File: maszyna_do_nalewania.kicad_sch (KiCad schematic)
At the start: 23 parts, among them J1 USB_C_Receptacle_USB2.0_16P, U1 ESP32-C3, Y1 40Mhz 10ppm

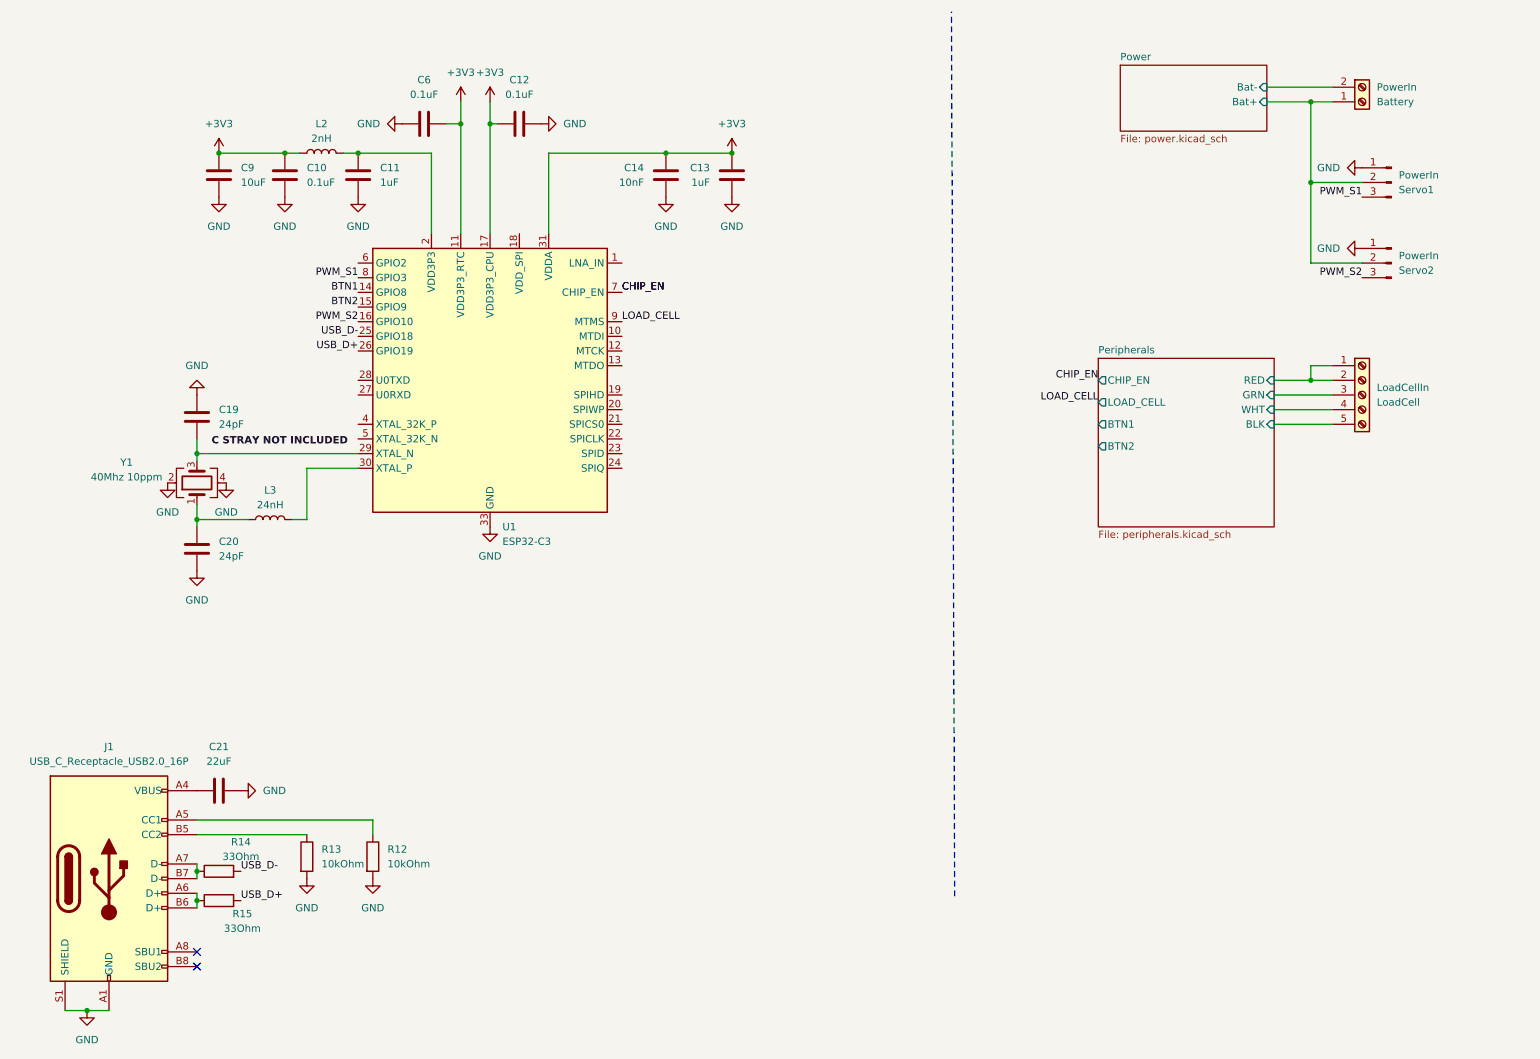
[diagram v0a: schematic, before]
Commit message: feat: led_inf connected, load cell overvoltage protection and antenna vals defined
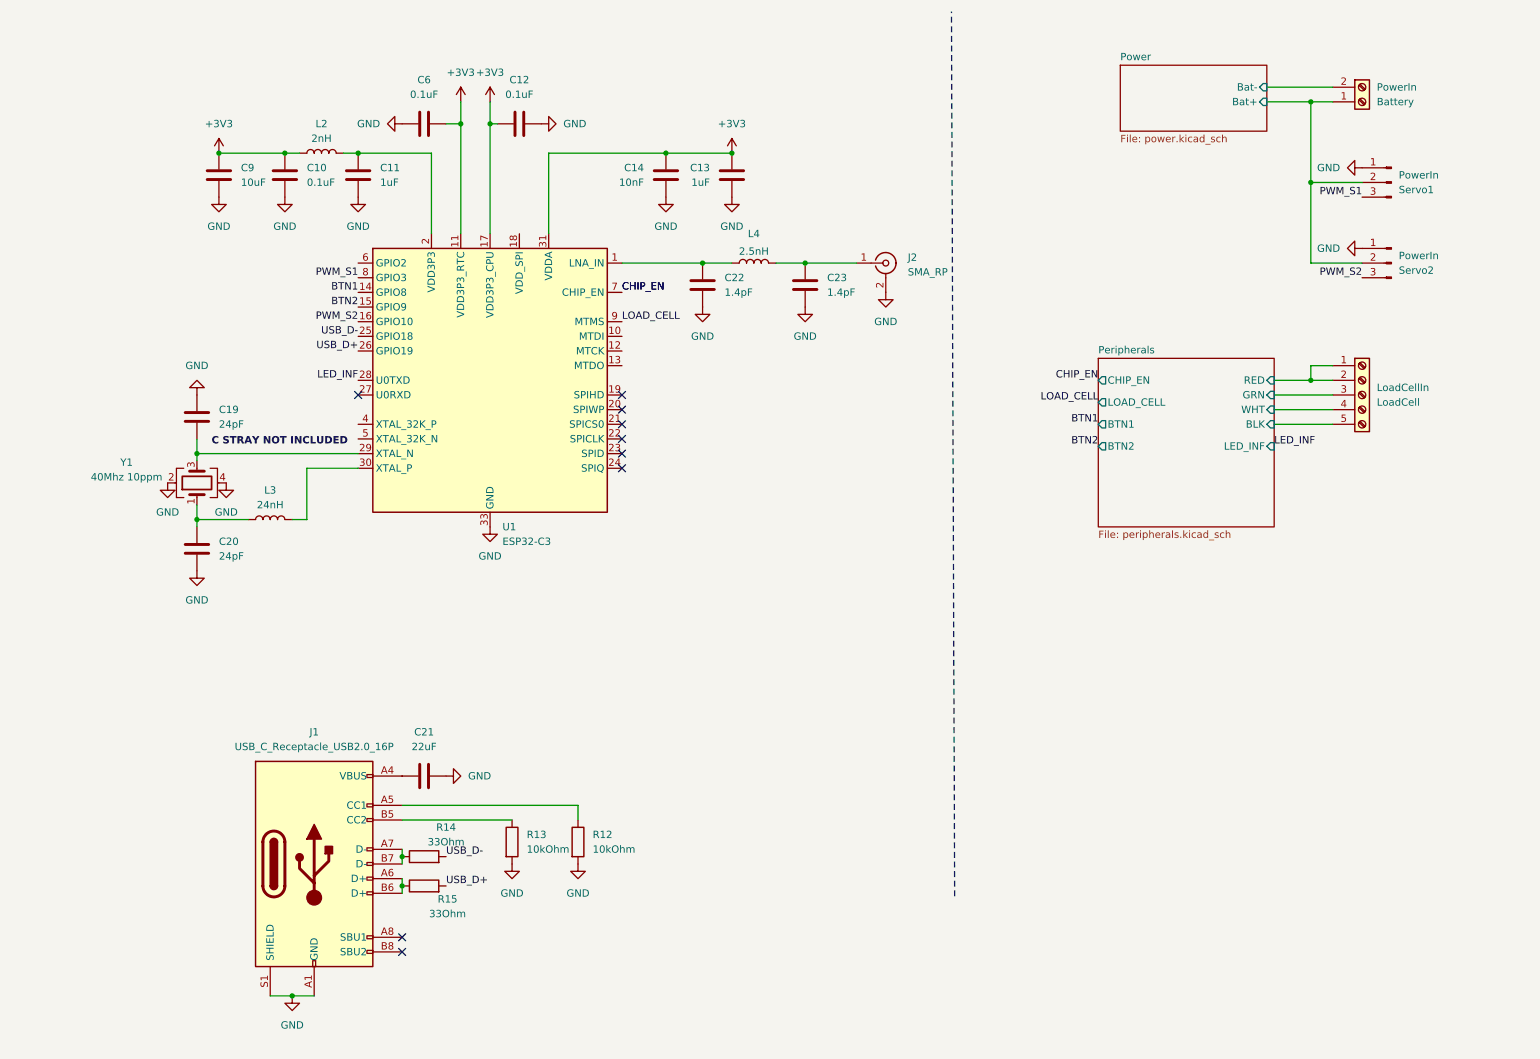
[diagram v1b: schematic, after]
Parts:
- added C22, C23: 1.4pF, Capacitor_SMD:C_0805_2012Metric_Pad1.18x1.45mm_HandSolder, symbol Device:C
- added J2: SMA_RP, Connector_Coaxial:SMA_Amphenol_132289_EdgeMount, symbol Connector:Conn_Coaxial
- added L4: 2.5nH, Inductor_SMD:L_0402_1005Metric_Pad0.77x0.64mm_HandSolder, symbol Device:L
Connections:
- net GND: now also C22.1, C23.1, J2.2 (Ext)
- net at U1.1 (LNA_IN): now also C22.2, L4.1
- net LED_INF: now reaches U1.28 (U0TXD)
- new net: C23.2, J2.1 (In), L4.2
- no-connect marks 2 -> 9
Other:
- sheet Peripherals ports: added LED_INF; removed none
- moved on the sheet: C21, J1, R12, R13, R14, R15

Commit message: feat: added power button, name changes
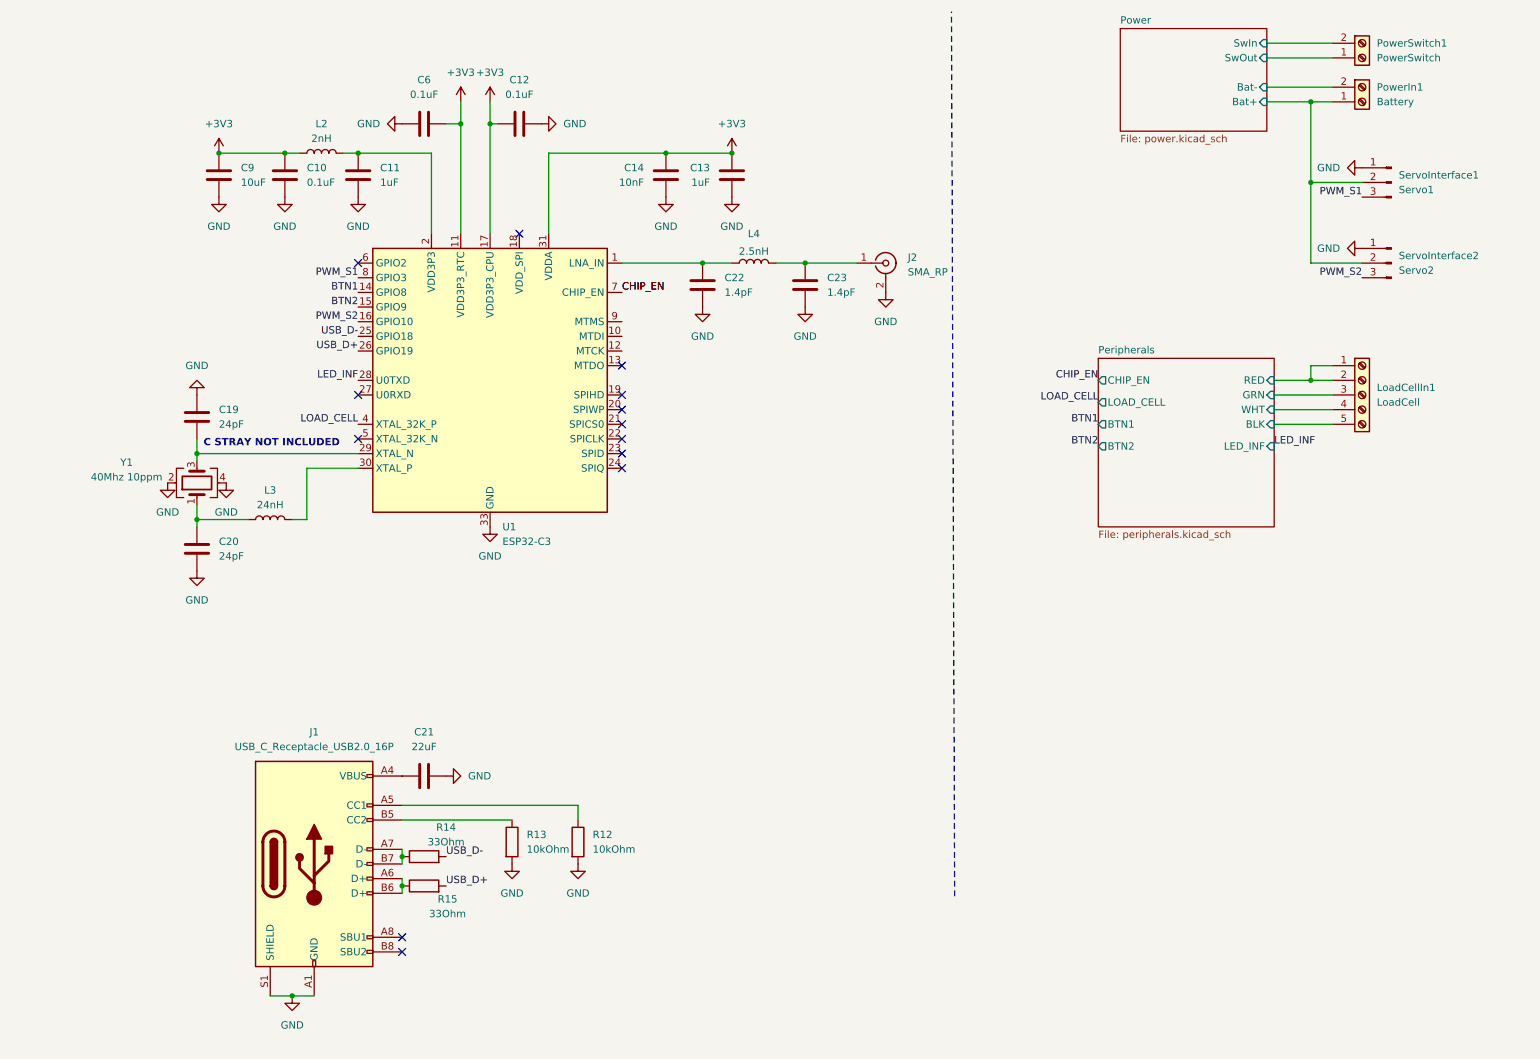
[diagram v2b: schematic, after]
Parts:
- removed LoadCellIn: LoadCell, symbol Connector:Screw_Terminal_01x05
- added LoadCellIn1: LoadCell, TerminalBlock:TerminalBlock_MaiXu_MX126-5.0-05P_1x05_P5.00mm, symbol Connector:Screw_Terminal_01x05
- added PowerSwitch1: PowerSwitch, TerminalBlock:TerminalBlock_MaiXu_MX126-5.0-02P_1x02_P5.00mm, symbol Connector:Screw_Terminal_01x02
- renumbered PowerIn to PowerIn1, PowerIn to ServoInterface1, PowerIn to ServoInterface2
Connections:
- net LOAD_CELL: now also U1.4 (XTAL_32K_P); no longer U1.9 (MTMS)
- net Peripherals/BLK: now also LoadCellIn1.5 (Pin_5)
- net Peripherals/GRN: now also LoadCellIn1.3 (Pin_3)
- net Peripherals/RED: now also LoadCellIn1.1 (Pin_1), LoadCellIn1.2 (Pin_2)
- net Peripherals/WHT: now also LoadCellIn1.4 (Pin_4)
- new net Power/SwIn: PowerSwitch1.2 (Pin_2)
- new net Power/SwOut: PowerSwitch1.1 (Pin_1)
- no-connect marks 9 -> 13
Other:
- sheet Power ports: added SwIn, SwOut; removed none
- note added: "C STRAY NOT INCLUDED"
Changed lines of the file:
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@@
 	(generator_version "9.0")
 	(paper "A4")
+	(text "C STRAY NOT INCLUDED"
+		(exclude_from_sim no)
+		(at 58.674 87.122 0)
+		(effects
+			(font
+				(size 1.27 1.27)
+				(thickness 0.254)
+				(bold yes)
+				(color 255 0 34 1)
+			)
+		)
+	)
 	(junction
 		(at 81.28 163.83)
@@
 	)
 	(no_connect
+		(at 73.66 86.36)
+	)
+	(no_connect
 		(at 73.66 78.74)
 	)
@@
 	)
 	(no_connect
+		(at 119.38 73.66)
+	)
+	(no_connect
 		(at 81.28 175.26)
 	)
@@
 	)
 	(no_connect
+		(at 73.66 55.88)
+	)
+	(no_connect
 		(at 81.28 172.72)
 	)
 	(no_connect
+		(at 101.6 50.8)
+	)
+	(no_connect
 		(at 119.38 81.28)
 	)
@@
 	(wire
 		(pts
+			(xy 231.14 17.78) (xy 242.57 17.78)
+		)
+		(stroke
+			(width 0)
+			(type default)
+		)
+	)
+	(wire
+		(pts
 			(xy 45.72 88.9) (xy 45.72 90.17)
 		)
@@
 	(wire
 		(pts
+			(xy 231.14 20.32) (xy 242.57 20.32)
+		)
+		(stroke
+			(width 0)
+			(type default)
+		)
+	)
+	(wire
+		(pts
 			(xy 64.77 91.44) (xy 73.66 91.44)
 		)
@@
 		)
 	)
-	(label "BTN1"
-		(at 73.66 60.96 180)
-		(effects
-			(font
-				(size 1.27 1.27)
-			)
-			(justify right bottom)
-		)
-	)
 	(label "LOAD_CELL"
-		(at 119.38 66.04 0)
+		(at 73.66 83.82 180)
 		(effects
 			(font
 				(size 1.27 1.27)
 			)
-			(justify left bottom)
+			(justify right bottom)
 		)
 	)
-	(label "C STRAY NOT INCLUDED"
-		(at 48.26 87.63 0)
+	(label "BTN1"
+		(at 73.66 60.96 180)
 		(effects
 			(font
 				(size 1.27 1.27)
-				(thickness 0.254)
-				(bold yes)
-				(color 255 0 34 1)
 			)
-			(justify left bottom)
+			(justify right bottom)
 		)
 	)
@@
 	)
 	(symbol
+		(lib_id "Connector:Screw_Terminal_01x05")
+		(at 247.65 78.74 0)
+		(unit 1)
+		(exclude_from_sim no)
+		(in_bom yes)
+		(on_board yes)
+		(dnp no)
+		(fields_autoplaced yes)
+		(property "Reference" "LoadCellIn1"
+			(at 250.19 77.4699 0)
+			(effects
+				(font
+					(size 1.27 1.27)
+				)
+				(justify left)
+			)
+		)
+		(property "Value" "LoadCell"
+			(at 250.19 80.0099 0)
+			(effects
+				(font
+					(size 1.27 1.27)
+				)
+				(justify left)
+			)
+		)
+		(property "Footprint" "TerminalBlock:TerminalBlock_MaiXu_MX126-5.0-05P_1x05_P5.00mm"
+			(at 247.65 78.74 0)
+			(effects
+				(font
+					(size 1.27 1.27)
+				)
+				(hide yes)
+			)
+		)
+		(property "Datasheet" "~"
+			(at 247.65 78.74 0)
+			(effects
+				(font
+					(size 1.27 1.27)
+				)
+				(hide yes)
+			)
+		)
+		(property "Description" "Generic screw terminal, single row, 01x05, script generated (kicad-library-utils/schlib/autogen/connector/)"
+			(at 247.65 78.74 0)
+			(effects
+				(font
+					(size 1.27 1.27)
+				)
+				(hide yes)
+			)
+		)
+		(pin "2"
+		)
+		(pin "4"
+		)
+		(pin "5"
+		)
+		(pin "1"
+		)
+		(pin "3"
+		)
+		(instances
+			(project ""
+				(path "/9edf3a40-33ab-40a8-8c54-e53c70f0a44f"
+					(reference "LoadCellIn1")
+					(unit 1)
+				)
+			)
+		)
+	)
+	(symbol
 		(lib_id "power:GND")
 		(at 138.43 44.45 0)
@@
 	)
 	(symbol
+		(lib_id "Connector:Screw_Terminal_01x02")
+		(at 247.65 17.78 0)
+		(unit 1)
+		(exclude_from_sim no)
+		(in_bom yes)
+		(on_board yes)
+		(dnp no)
+		(fields_autoplaced yes)
+		(property "Reference" "PowerSwitch1"
+			(at 250.19 17.7799 0)
+			(effects
+				(font
+					(size 1.27 1.27)
+				)
+				(justify left)
+			)
+		)
+		(property "Value" "PowerSwitch"
+			(at 250.19 20.3199 0)
+			(effects
+				(font
+					(size 1.27 1.27)
+				)
+				(justify left)
+			)
+		)
+		(property "Footprint" "TerminalBlock:TerminalBlock_MaiXu_MX126-5.0-02P_1x02_P5.00mm"
+			(at 247.65 17.78 0)
+			(effects
+				(font
+					(size 1.27 1.27)
+				)
+				(hide yes)
+			)
+		)
+		(property "Datasheet" "~"
+			(at 247.65 17.78 0)
+			(effects
+				(font
+					(size 1.27 1.27)
+				)
+				(hide yes)
+			)
+		)
+		(property "Description" "Generic screw terminal, single row, 01x02, script generated (kicad-library-utils/schlib/autogen/connector/)"
+			(at 247.65 17.78 0)
+			(effects
+				(font
+					(size 1.27 1.27)
+				)
+				(hide yes)
+			)
+		)
+		(pin "1"
+		)
+		(pin "2"
+		)
+		(instances
+			(project "maszyna_do_nalewania"
+				(path "/9edf3a40-33ab-40a8-8c54-e53c70f0a44f"
+					(reference "PowerSwitch1")
+					(unit 1)
+				)
+			)
+		)
+	)
+	(symbol
 		(lib_id "power:GND")
 		(at 62.23 182.88 0)
@@
 		(dnp no)
 		(fields_autoplaced yes)
-		(property "Reference" "PowerIn"
+		(property "Reference" "PowerIn1"
 			(at 250.19 25.3999 0)
 			(effects
@@
 			(project ""
 				(path "/9edf3a40-33ab-40a8-8c54-e53c70f0a44f"
-					(reference "PowerIn")
+					(reference "PowerIn1")
 					(unit 1)
 				)
@@
 	)
 	(symbol
-		(lib_id "Connector:Screw_Terminal_01x05")
-		(at 247.65 78.74 0)
-		(unit 1)
-		(exclude_from_sim no)
-		(in_bom yes)
-		(on_board yes)
-		(dnp no)
-		(fields_autoplaced yes)
-		(property "Reference" "LoadCellIn"
-			(at 250.19 77.4699 0)
-			(effects
-				(font
-					(size 1.27 1.27)
-				)
-				(justify left)
-			)
-		)
-		(property "Value" "LoadCell"
-			(at 250.19 80.0099 0)
-			(effects
-				(font
-					(size 1.27 1.27)
-				)
-				(justify left)
-			)
-		)
-		(property "Footprint" ""
-			(at 247.65 78.74 0)
-			(effects
-				(font
-					(size 1.27 1.27)
-				)
-				(hide yes)
-			)
-		)
-		(property "Datasheet" "~"
-			(at 247.65 78.74 0)
-			(effects
-				(font
-					(size 1.27 1.27)
-				)
-				(hide yes)
-			)
-		)
-		(property "Description" "Generic screw terminal, single row, 01x05, script generated (kicad-library-utils/schlib/autogen/connector/)"
-			(at 247.65 78.74 0)
-			(effects
-				(font
-					(size 1.27 1.27)
-				)
-				(hide yes)
-			)
-		)
-		(pin "4"
-		)
-		(pin "2"
-		)
-		(pin "3"
-		)
-		(pin "1"
-		)
-		(pin "5"
-		)
-		(instances
-			(project ""
-				(path "/9edf3a40-33ab-40a8-8c54-e53c70f0a44f"
-					(reference "LoadCellIn")
-					(unit 1)
-				)
-			)
-		)
-	)
-	(symbol
 		(lib_id "power:GND")
 		(at 247.65 39.37 270)
@@
 		(dnp no)
 		(fields_autoplaced yes)
-		(property "Reference" "PowerIn"
+		(property "Reference" "ServoInterface2"
 			(at 254 54.6099 0)
 			(effects
@@
 			(project "maszyna_do_nalewania"
 				(path "/9edf3a40-33ab-40a8-8c54-e53c70f0a44f"
-					(reference "PowerIn")
+					(reference "ServoInterface2")
 					(unit 1)
 				)
@@
 		(dnp no)
 		(fields_autoplaced yes)
-		(property "Reference" "PowerIn"
+		(property "Reference" "ServoInterface1"
 			(at 254 40.6399 0)
 			(effects
@@
 			(project ""
 				(path "/9edf3a40-33ab-40a8-8c54-e53c70f0a44f"
-					(reference "PowerIn")
+					(reference "ServoInterface1")
 					(unit 1)
 				)
@@
 	)
 	(sheet
-		(at 205.74 21.59)
-		(size 25.4 11.43)
+		(at 205.74 15.24)
+		(size 25.4 17.78)
 		(exclude_from_sim no)
 		(in_bom yes)
@@
 		)
 		(property "Sheetname" "Power"
-			(at 205.74 20.8784 0)
+			(at 205.74 14.5284 0)
 			(show_name yes)
 			(effects
@@
 			(effects
 				(font
+					(size 1.27 1.27)
+				)
+				(justify right)
+			)
+		)
+		(pin "SwIn" input
+			(at 231.14 17.78 0)
+			(effects
+				(font
+					(size 1.27 1.27)
+				)
+				(justify right)
+			)
+		)
+		(pin "SwOut" input
+			(at 231.14 20.32 0)
+			(effects
+				(font

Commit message: wip: pcb layout started
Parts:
- removed PowerIn1: Battery, TerminalBlock:TerminalBlock_MaiXu_MX126-5.0-02P_1x02_P5.00mm, symbol Connector:Screw_Terminal_01x02
- removed PowerSwitch1: PowerSwitch, TerminalBlock:TerminalBlock_MaiXu_MX126-5.0-02P_1x02_P5.00mm, symbol Connector:Screw_Terminal_01x02
- added PowerIn1: Battery-, TerminalBlock_MetzConnect:TerminalBlock_MetzConnect_360271_1x01_Horizontal_ScrewM3.0_Boxed, symbol Connector:Screw_Terminal_01x01
- added PowerIn2: Battery+, TerminalBlock_MetzConnect:TerminalBlock_MetzConnect_360271_1x01_Horizontal_ScrewM3.0_Boxed, symbol Connector:Screw_Terminal_01x01
- added PowerSwitch1, PowerSwitch2: Screw_Terminal_01x01, TerminalBlock_MetzConnect:TerminalBlock_MetzConnect_360271_1x01_Horizontal_ScrewM3.0_Boxed, symbol Connector:Screw_Terminal_01x01
- R14: footprint Resistor_SMD:R_0402_1005Metric_Pad0.72x0.64mm_HandSolder -> Resistor_SMD:R_0402_1005Metric
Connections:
- net Power/Bat+: now also PowerIn2.1 (Pin_1)
- net Power/Bat-: now also PowerIn1.1 (Pin_1)
- net Power/SwIn: now also PowerSwitch1.1 (Pin_1)
- net Power/SwOut: now also PowerSwitch2.1 (Pin_1)
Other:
- moved on the sheet: ServoInterface1, ServoInterface2
